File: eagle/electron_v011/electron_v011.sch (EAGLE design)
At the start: 92 parts, among them J1 SIM-NANO-4FF, J2 IPEX-20279-001E, U1 U-BLOX-SARA-U260, U2 SN74AVC4T245, U3 STM32F205RG, U4 MAX1704X, U5 SN74LVC1G07, U6 SN74LVC1G07, U8 SN74AVC4T245, X1 USB-MICROB, Y1 32Khz, Y2 26Mhz

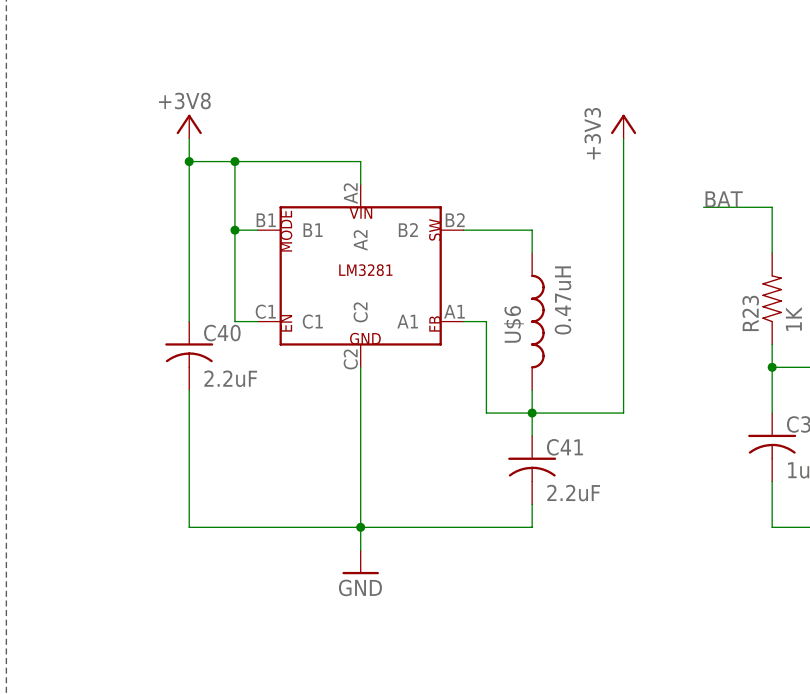
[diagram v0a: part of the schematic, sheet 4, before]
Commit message: Replaced LM3281 with TPS62291 in schematic and updated circuit
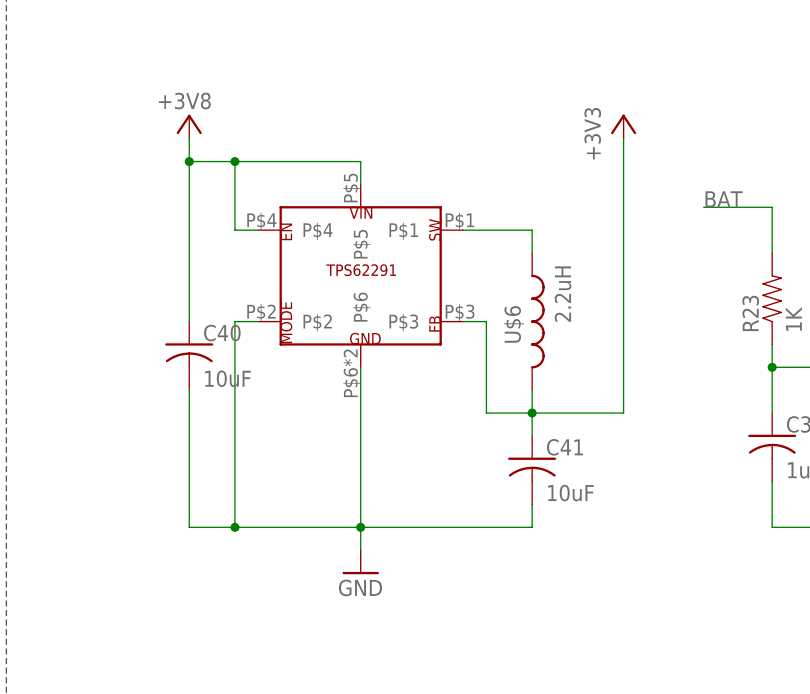
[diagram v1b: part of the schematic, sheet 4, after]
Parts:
- C40, C41: value 2.2uF -> 10uF
- U$5: value (none) -> TPS62291DRV; device Particle:LM3281_DSBGA -> Particle:TPS62291DRV
- U$6: value 0.47uH -> 2.2uH
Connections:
- net +3V3: now also U$5.P$3; no longer U$5.A1
- net +3V8: now also U$5.P$4, U$5.P$5; no longer U$5.A2, U$5.B1, U$5.C1
- net GND: now also U$5.P$2, U$5.P$6; no longer U$5.C2
- net N$3: now also U$5.P$1; no longer U$5.B2
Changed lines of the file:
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@@
 <part name="R19" library="Spark" deviceset="R-US_" device="" value="10K"/>
 <part name="C7" library="Spark" deviceset="C-US" device="" value="47nF"/>
-<part name="U$6" library="Particle" deviceset="INDUCTOR" device="G" value="0.47uH"/>
-<part name="C40" library="Bretts-Spark-Library" deviceset="C-US" device="0603" value="2.2uF"/>
-<part name="C41" library="Bretts-Spark-Library" deviceset="C-US" device="0603" value="2.2uF"/>
+<part name="U$6" library="Particle" deviceset="INDUCTOR" device="G" value="2.2uH"/>
+<part name="C40" library="Bretts-Spark-Library" deviceset="C-US" device="0603" value="10uF"/>
+<part name="C41" library="Bretts-Spark-Library" deviceset="C-US" device="0603" value="10uF"/>
 <part name="C4" library="Bretts-Spark-Library" deviceset="C-US" device="0603" value="1uF"/>
 <part name="C5" library="Bretts-Spark-Library" deviceset="C-US" device="0603" value="20uF"/>
@@
 <part name="R23" library="SparkFun-Passives" deviceset="RESISTOR" device="0603-RES" value="1K"/>
 <part name="+3V13" library="supply1" deviceset="+3V3" device=""/>
-<part name="U$5" library="Particle" deviceset="LM3281" device="_DSBGA"/>
 <part name="GND38" library="supply1" deviceset="GND" device=""/>
 <part name="+3V15" library="supply1" deviceset="+3V3" device="" value="+3V8"/>
@@
 <part name="JP3" library="Particle" deviceset="PINHD-1X1" device=""/>
 <part name="JP2" library="Particle" deviceset="M18" device="DPAD"/>
+<part name="U$5" library="Particle" deviceset="TPS62291" device="DRV"/>
 </parts>
 <sheets>
@@
 <instance part="R23" gate="G$1" x="171.45" y="135.89" rot="R90"/>
 <instance part="+3V13" gate="G$1" x="180.34" y="156.21"/>
-<instance part="U$5" gate="G$1" x="125.73" y="138.43"/>
 <instance part="GND38" gate="1" x="125.73" y="105.41"/>
 <instance part="+3V15" gate="G$1" x="106.68" y="156.21" smashed="yes">
@@
 <attribute name="VALUE" x="172.974" y="115.951" size="1.778" layer="96"/>
 </instance>
+<instance part="U$5" gate="G$1" x="125.73" y="138.43"/>
 </instances>
 <busses>
@@
 <wire x1="154.94" y1="123.19" x2="144.78" y2="123.19" width="0.1524" layer="91"/>
 <junction x="144.78" y="123.19"/>
-<pinref part="U$5" gate="G$1" pin="A1"/>
 <wire x1="137.16" y1="133.35" x2="139.7" y2="133.35" width="0.1524" layer="91"/>
 <wire x1="139.7" y1="133.35" x2="139.7" y2="123.19" width="0.1524" layer="91"/>
 <wire x1="139.7" y1="123.19" x2="144.78" y2="123.19" width="0.1524" layer="91"/>
+<pinref part="U$5" gate="G$1" pin="P$3"/>
 </segment>
 </net>
@@
 <pinref part="C40" gate="G$1" pin="2"/>
 <wire x1="106.68" y1="125.73" x2="106.68" y2="110.49" width="0.1524" layer="91"/>
-<wire x1="106.68" y1="110.49" x2="125.73" y2="110.49" width="0.1524" layer="91"/>
+<wire x1="106.68" y1="110.49" x2="111.76" y2="110.49" width="0.1524" layer="91"/>
 <pinref part="C41" gate="G$1" pin="2"/>
+<wire x1="111.76" y1="110.49" x2="125.73" y2="110.49" width="0.1524" layer="91"/>
 <wire x1="125.73" y1="110.49" x2="144.78" y2="110.49" width="0.1524" layer="91"/>
 <wire x1="144.78" y1="110.49" x2="144.78" y2="113.03" width="0.1524" layer="91"/>
@@
 <wire x1="125.73" y1="107.95" x2="125.73" y2="110.49" width="0.1524" layer="91"/>
 <junction x="125.73" y="110.49"/>
-<pinref part="U$5" gate="G$1" pin="C2"/>
 <wire x1="125.73" y1="128.27" x2="125.73" y2="110.49" width="0.1524" layer="91"/>
+<pinref part="U$5" gate="G$1" pin="P$6"/>
+<pinref part="U$5" gate="G$1" pin="P$2"/>
+<wire x1="114.3" y1="133.35" x2="111.76" y2="133.35" width="0.1524" layer="91"/>
+<wire x1="111.76" y1="133.35" x2="111.76" y2="110.49" width="0.1524" layer="91"/>
+<junction x="111.76" y="110.49"/>
 </segment>
 <segment>
@@
 <pinref part="C40" gate="G$1" pin="1"/>
 <wire x1="106.68" y1="153.67" x2="106.68" y2="151.13" width="0.1524" layer="91"/>
-<pinref part="U$5" gate="G$1" pin="A2"/>
 <wire x1="106.68" y1="151.13" x2="106.68" y2="133.35" width="0.1524" layer="91"/>
 <wire x1="125.73" y1="148.59" x2="125.73" y2="151.13" width="0.1524" layer="91"/>
 <wire x1="125.73" y1="151.13" x2="111.76" y2="151.13" width="0.1524" layer="91"/>
 <junction x="106.68" y="151.13"/>
-<pinref part="U$5" gate="G$1" pin="C1"/>
 <wire x1="111.76" y1="151.13" x2="106.68" y2="151.13" width="0.1524" layer="91"/>
-<wire x1="114.3" y1="133.35" x2="111.76" y2="133.35" width="0.1524" layer="91"/>
-<wire x1="111.76" y1="133.35" x2="111.76" y2="143.51" width="0.1524" layer="91"/>
 <junction x="111.76" y="151.13"/>
-<pinref part="U$5" gate="G$1" pin="B1"/>
 <wire x1="111.76" y1="143.51" x2="111.76" y2="151.13" width="0.1524" layer="91"/>
 <wire x1="114.3" y1="143.51" x2="111.76" y2="143.51" width="0.1524" layer="91"/>
-<junction x="111.76" y="143.51"/>
+<pinref part="U$5" gate="G$1" pin="P$4"/>
+<pinref part="U$5" gate="G$1" pin="P$5"/>
 </segment>
 </net>
@@
 <net name="N$3" class="0">
 <segment>
-<pinref part="U$5" gate="G$1" pin="B2"/>
 <pinref part="U$6" gate="G$1" pin="1"/>
 <wire x1="137.16" y1="143.51" x2="144.78" y2="143.51" width="0.1524" layer="91"/>
 <wire x1="144.78" y1="143.51" x2="144.78" y2="140.97" width="0.1524" layer="91"/>
-</segment>
-</net>
+<pinref part="U$5" gate="G$1" pin="P$1"/>
+</segment>
+</net>

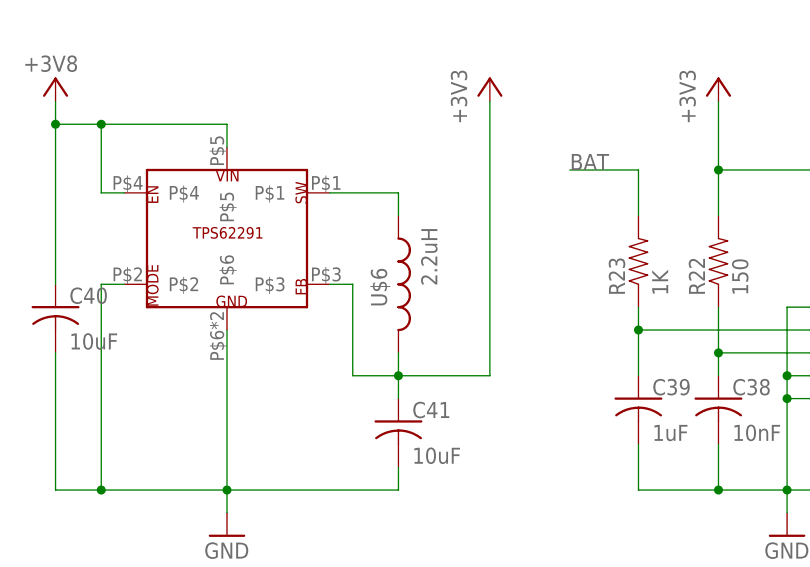
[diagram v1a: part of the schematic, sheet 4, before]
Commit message: 2.2uH inductor reused for 3.3V circuit, components placed and locked
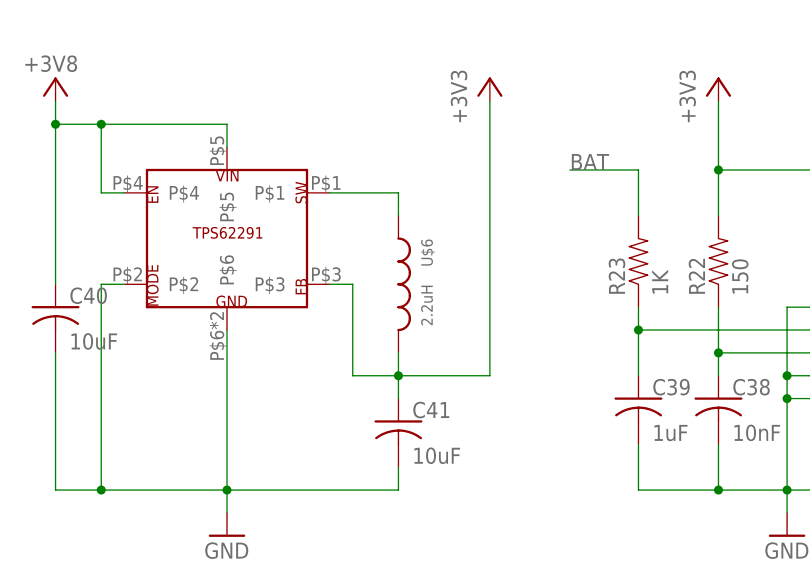
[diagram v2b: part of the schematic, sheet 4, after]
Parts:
- U$6: device Particle:INDUCTORG -> Particle:INDUCTORH
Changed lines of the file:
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@@
 <part name="R19" library="Spark" deviceset="R-US_" device="" value="10K"/>
 <part name="C7" library="Spark" deviceset="C-US" device="" value="47nF"/>
-<part name="U$6" library="Particle" deviceset="INDUCTOR" device="G" value="2.2uH"/>
 <part name="C40" library="Bretts-Spark-Library" deviceset="C-US" device="0603" value="10uF"/>
 <part name="C41" library="Bretts-Spark-Library" deviceset="C-US" device="0603" value="10uF"/>
@@
 <part name="JP2" library="Particle" deviceset="M18" device="DPAD"/>
 <part name="U$5" library="Particle" deviceset="TPS62291" device="DRV"/>
+<part name="U$6" library="Particle" deviceset="INDUCTOR" device="H" value="2.2uH"/>
 </parts>
 <sheets>
@@
 <attribute name="VALUE" x="81.026" y="64.389" size="1.778" layer="96" rot="R180"/>
 </instance>
-<instance part="U$6" gate="G$1" x="144.78" y="133.35" smashed="yes">
-<attribute name="NAME" x="143.51" y="130.81" size="1.778" layer="95" rot="R90"/>
-<attribute name="VALUE" x="147.32" y="139.7" size="1.778" layer="96" rot="R270"/>
-</instance>
 <instance part="C40" gate="G$1" x="106.68" y="130.81" smashed="yes">
 <attribute name="NAME" x="108.204" y="131.191" size="1.778" layer="95"/>
@@
 </instance>
 <instance part="U$5" gate="G$1" x="125.73" y="138.43"/>
+<instance part="U$6" gate="G$1" x="144.78" y="133.35" smashed="yes">
+<attribute name="NAME" x="147.32" y="138.43" size="1.27" layer="95" rot="R270"/>
+<attribute name="VALUE" x="147.32" y="133.35" size="1.27" layer="96" rot="R270"/>
+</instance>
 </instances>
 <busses>
@@
 <pinref part="+3V18" gate="G$1" pin="+3V3"/>
 <wire x1="154.94" y1="153.67" x2="154.94" y2="123.19" width="0.1524" layer="91"/>
-<pinref part="U$6" gate="G$1" pin="2"/>
 <pinref part="C41" gate="G$1" pin="1"/>
 <wire x1="144.78" y1="125.73" x2="144.78" y2="123.19" width="0.1524" layer="91"/>
@@
 <wire x1="139.7" y1="123.19" x2="144.78" y2="123.19" width="0.1524" layer="91"/>
 <pinref part="U$5" gate="G$1" pin="P$3"/>
+<pinref part="U$6" gate="G$1" pin="2"/>
 </segment>
 </net>
@@
 <net name="N$3" class="0">
 <segment>
-<pinref part="U$6" gate="G$1" pin="1"/>
 <wire x1="137.16" y1="143.51" x2="144.78" y2="143.51" width="0.1524" layer="91"/>
 <wire x1="144.78" y1="143.51" x2="144.78" y2="140.97" width="0.1524" layer="91"/>
 <pinref part="U$5" gate="G$1" pin="P$1"/>
-</segment>
-</net>
+<pinref part="U$6" gate="G$1" pin="1"/>
+</segment>
+</net>

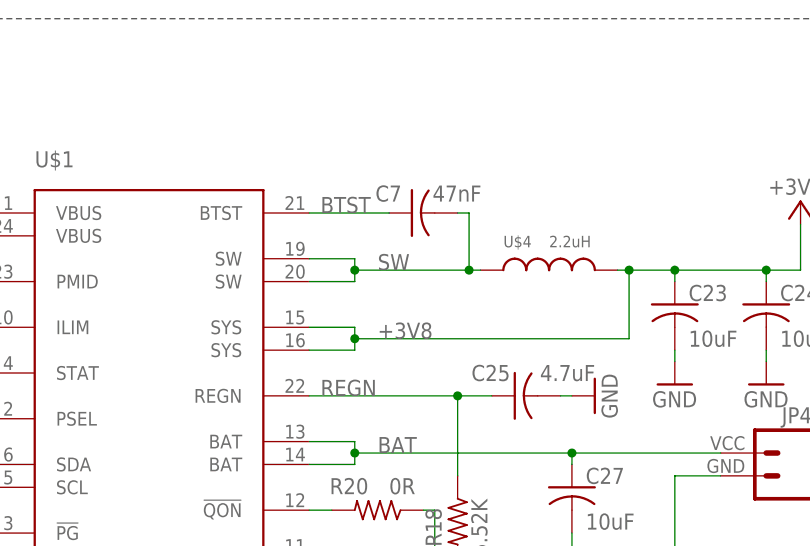
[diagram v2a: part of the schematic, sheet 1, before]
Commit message: Completed v011 PCB routing for revised 3.3V power circuit #19
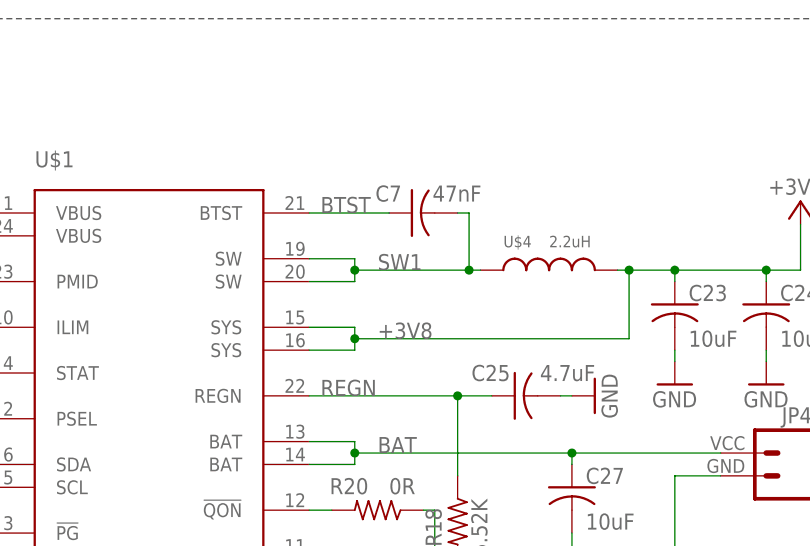
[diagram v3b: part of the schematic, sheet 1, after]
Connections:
- net N$3 renamed SW2
- net SW renamed SW1
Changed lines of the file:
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@@
 </segment>
 </net>
-<net name="SW" class="0">
+<net name="SW1" class="0">
 <segment>
 <pinref part="U$1" gate="G$1" pin="SW@20"/>
@@
 </segment>
 </net>
-<net name="N$3" class="0">
+<net name="SW2" class="0">
 <segment>
 <wire x1="137.16" y1="143.51" x2="144.78" y2="143.51" width="0.1524" layer="91"/>
@@
 <pinref part="U$5" gate="G$1" pin="P$1"/>
 <pinref part="U$6" gate="G$1" pin="1"/>
-</segment>
-</net>
+<label x="139.7" y="143.51" size="1.778" layer="95"/>
+</segment>
+</net>
